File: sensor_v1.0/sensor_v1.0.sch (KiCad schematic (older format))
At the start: 4 parts

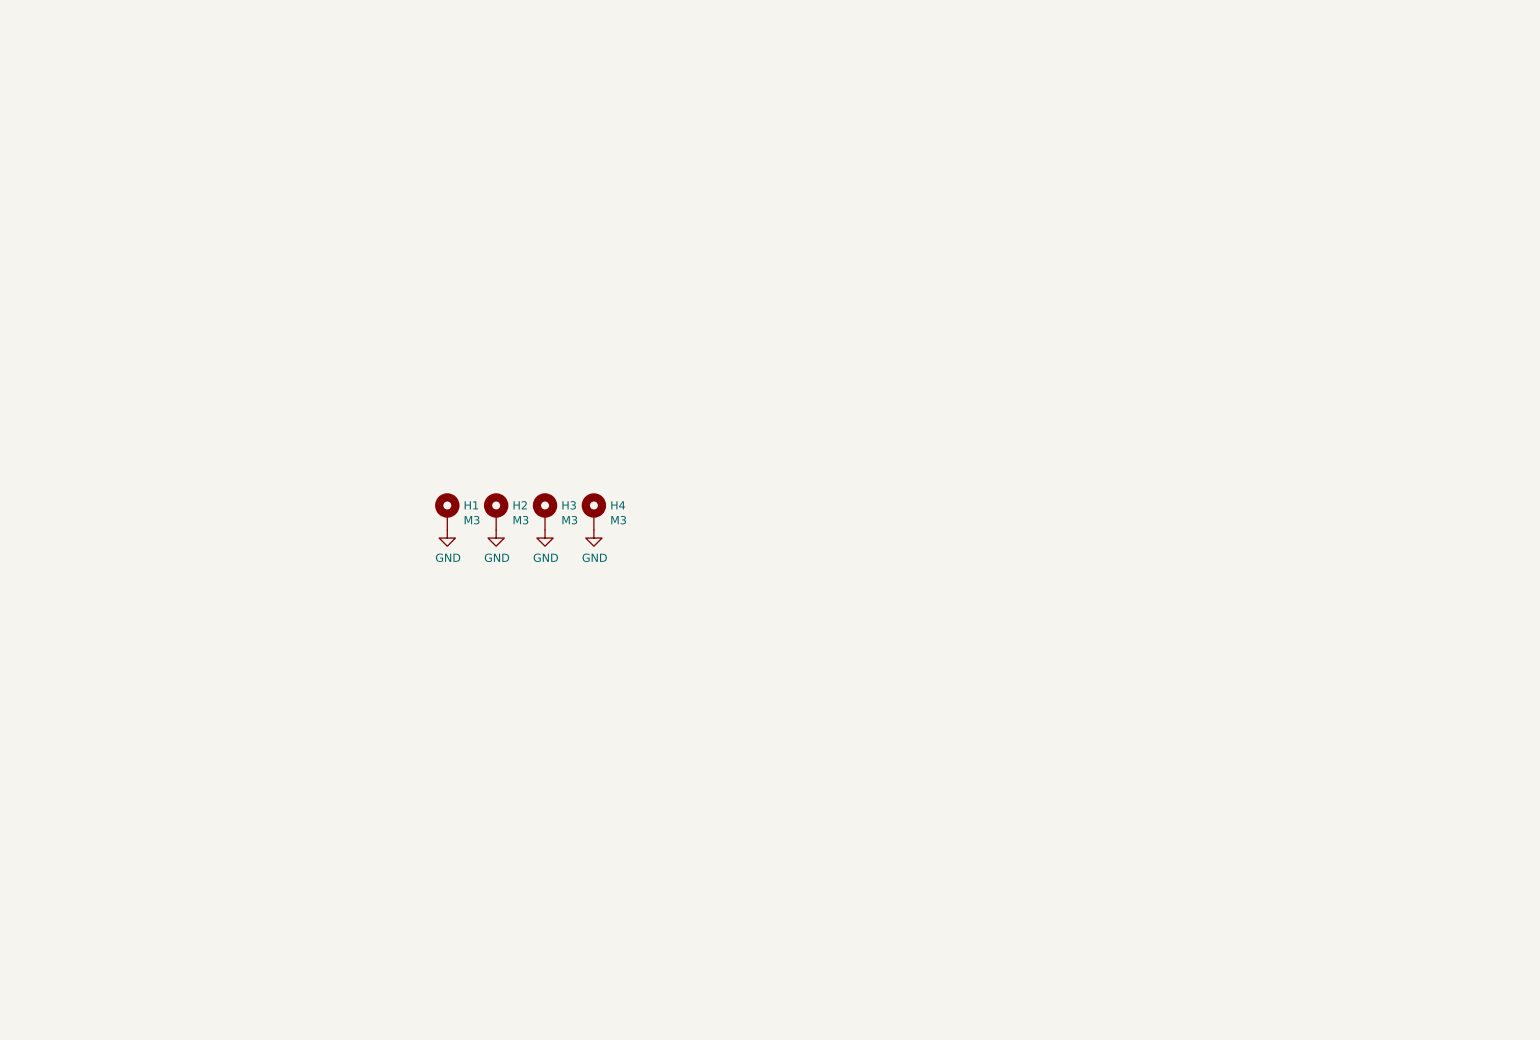
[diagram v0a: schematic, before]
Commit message: sensor board v1.0 mostly routed
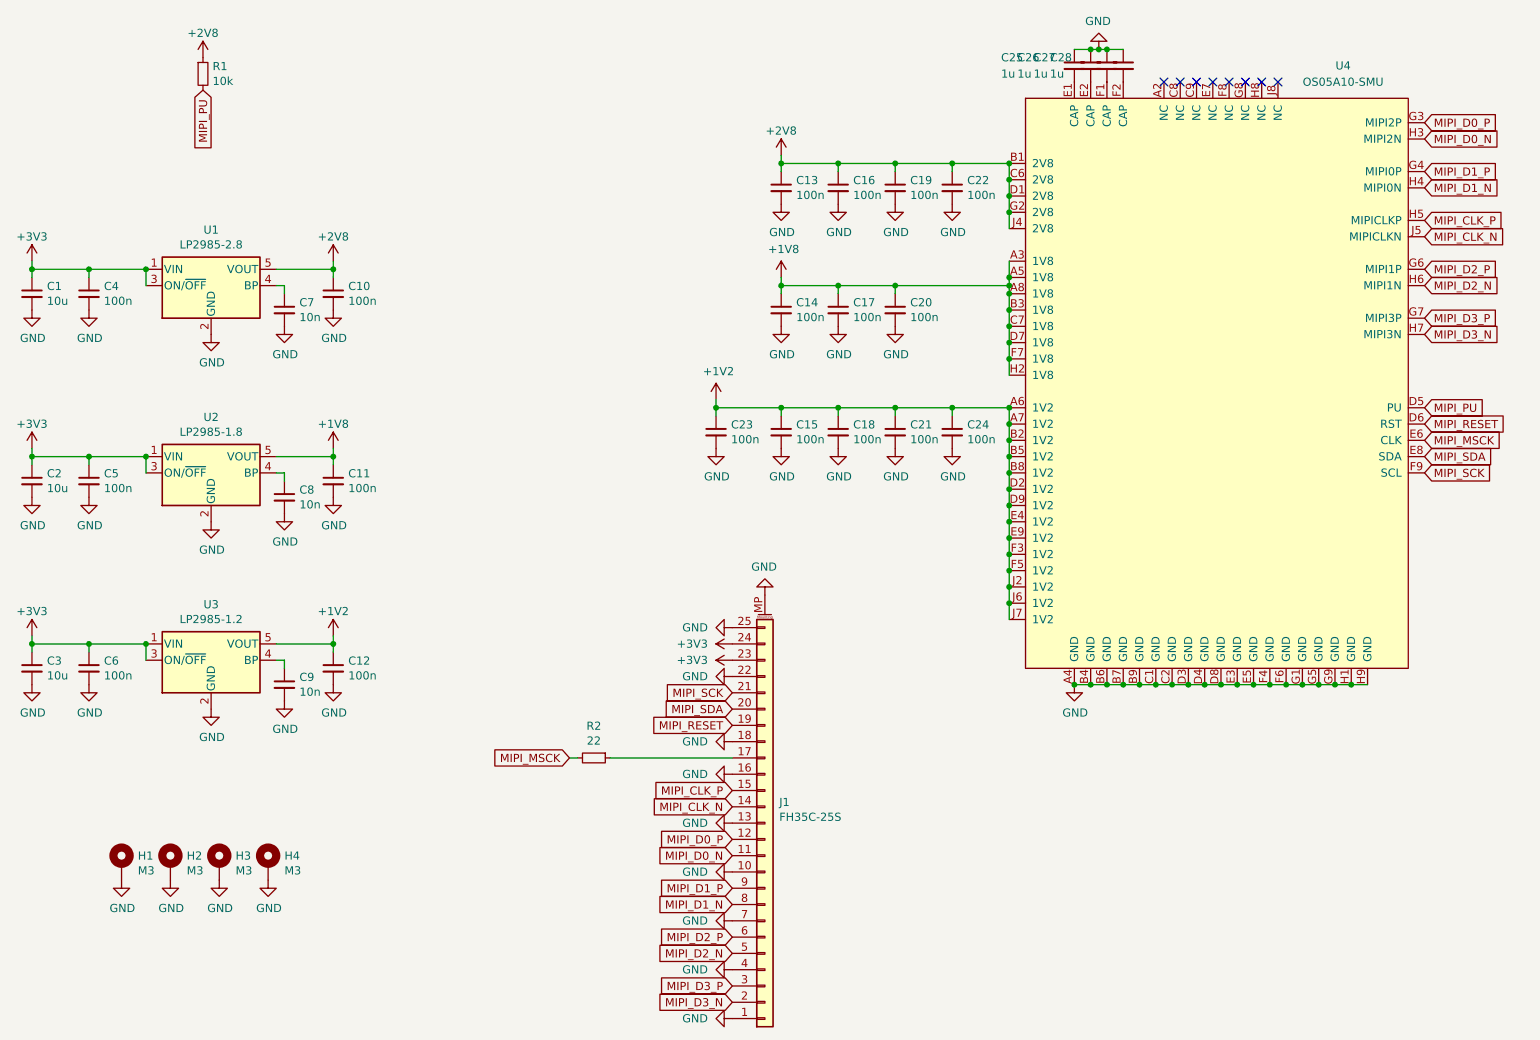
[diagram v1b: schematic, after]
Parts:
- added C1, C2, C3: 10u, otter:C_0603, symbol Device:C_Small
- added C10, C11, C12, C13, C14, C15, C16, C17, C18, C19, C20, C21, C22, C23, C24, C4, C5, C6: 100n, otter:C_0402, symbol Device:C_Small
- added C25, C26, C27, C28: 1u, otter:C_0402, symbol Device:C_Small
- added C7, C8, C9: 10n, otter:C_0402, symbol Device:C_Small
- added J1: FH35C-25S, otter:FH35C-25S, symbol Connector_Generic_MountingPin:Conn_01x25_MountingPin
- added R1: 10k, otter:R_0402, symbol Device:R_Small
- added R2: 22, otter:R_0402, symbol Device:R_Small
- added U1: LP2985-2.8, Package_TO_SOT_SMD:SOT-23-5, symbol Regulator_Linear:LP2985-2.8
- added U2: LP2985-1.8, Package_TO_SOT_SMD:SOT-23-5, symbol Regulator_Linear:LP2985-1.8
- added U3: LP2985-1.2, Package_TO_SOT_SMD:SOT-23-5, symbol Regulator_Linear:LP2985-1.8
- added U4: OS05A10-SMU, otter:OS05A10, symbol otter:OS05A10-SMU
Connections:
- net GND: now also C1.2, C10.2, C11.2, C12.2, C13.2, C14.2, C15.2, C16.2, C17.2, C18.2, C19.2, C2.2, C20.2, C21.2, C22.2, C23.2, C24.2, C25.1, C26.1, C27.1, C28.1, C3.2, C4.2, C5.2, C6.2, C7.2, C8.2, C9.2, J1.1 (Pin_1), J1.10 (Pin_10), J1.13 (Pin_13), J1.16 (Pin_16), J1.18 (Pin_18), J1.22 (Pin_22), J1.25 (Pin_25), J1.4 (Pin_4), J1.7 (Pin_7), J1.MP (MountPin), U1.2 (GND), U2.2 (GND), U3.2 (GND), U4.A4 (GND), U4.B4 (GND), U4.B6 (GND), U4.B7 (GND), U4.B9 (GND), U4.C1 (GND), U4.C2 (GND), U4.D3 (GND), U4.D4 (GND), U4.D8 (GND), U4.E3 (GND), U4.E5 (GND), U4.F4 (GND), U4.F6 (GND), U4.G1 (GND), U4.G5 (GND), U4.G9 (GND), U4.H1 (GND), U4.H9 (GND)
- new net: C25.2, U4.E1 (CAP)
- new net: C26.2, U4.E2 (CAP)
- new net: C27.2, U4.F1 (CAP)
- new net: C28.2, U4.F2 (CAP)
- new net: J1.17 (Pin_17), R2.1
- new net: C7.1, U1.4 (BP)
- new net: C8.1, U2.4 (BP)
- new net: C9.1, U3.4 (BP)
- new net +1V2: C12.1, C15.1, C18.1, C21.1, C23.1, C24.1, U3.5 (VOUT), U4.A6 (1V2), U4.A7 (1V2), U4.B2 (1V2), U4.B5 (1V2), U4.B8 (1V2), U4.D2 (1V2), U4.D9 (1V2), U4.E4 (1V2), U4.E9 (1V2), U4.F3 (1V2), U4.F5 (1V2), U4.J2 (1V2), U4.J6 (1V2), U4.J7 (1V2)
- new net +1V8: C11.1, C14.1, C17.1, C20.1, U2.5 (VOUT), U4.A3 (1V8), U4.A5 (1V8), U4.A8 (1V8), U4.B3 (1V8), U4.C7 (1V8), U4.D7 (1V8), U4.F7 (1V8), U4.H2 (1V8)
- new net +2V8: C10.1, C13.1, C16.1, C19.1, C22.1, R1.1, U1.5 (VOUT), U4.B1 (2V8), U4.C6 (2V8), U4.D1 (2V8), U4.G2 (2V8), U4.J4 (2V8)
- new net +3V3: C1.1, C2.1, C3.1, C4.1, C5.1, C6.1, J1.23 (Pin_23), J1.24 (Pin_24), U1.1 (VIN), U1.3 (ON/~OFF~), U2.1 (VIN), U2.3 (ON/~OFF~), U3.1 (VIN), U3.3 (ON/~OFF~)
- new net MIPI_CLK_N: J1.14 (Pin_14), U4.J5 (MIPICLKN)
- new net MIPI_CLK_P: J1.15 (Pin_15), U4.H5 (MIPICLKP)
- new net MIPI_D0_N: J1.11 (Pin_11), U4.H3 (MIPI2N)
- new net MIPI_D0_P: J1.12 (Pin_12), U4.G3 (MIPI2P)
- new net MIPI_D1_N: J1.8 (Pin_8), U4.H4 (MIPI0N)
- new net MIPI_D1_P: J1.9 (Pin_9), U4.G4 (MIPI0P)
- new net MIPI_D2_N: J1.5 (Pin_5), U4.H6 (MIPI1N)
- new net MIPI_D2_P: J1.6 (Pin_6), U4.G6 (MIPI1P)
- new net MIPI_D3_N: J1.2 (Pin_2), U4.H7 (MIPI3N)
- new net MIPI_D3_P: J1.3 (Pin_3), U4.G7 (MIPI3P)
- new net MIPI_MSCK: R2.2, U4.E6 (CLK)
- new net MIPI_PU: R1.2, U4.D5 (PU)
- new net MIPI_RESET: J1.19 (Pin_19), U4.D6 (RST)
- new net MIPI_SCK: J1.21 (Pin_21), U4.F9 (SCL)
- new net MIPI_SDA: J1.20 (Pin_20), U4.E8 (SDA)
- no-connect marks 0 -> 8
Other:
- moved on the sheet: H1, H2, H3, H4

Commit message: routing 100%
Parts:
- removed C13: 100n, otter:C_0402, symbol Device:C_Small
- added C29: 100n, otter:C_0402, symbol Device:C_Small
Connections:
- net +1V2: now also C29.1
- net GND: now also C29.2
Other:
- moved on the sheet: C16, C19, C22, C23
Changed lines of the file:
@@
 L power:+1V2 #PWR0121
 U 1 1 6099D00B
-P 5000 3500
-F 0 "#PWR0121" H 5000 3350 50  0001 C CNN
-F 1 "+1V2" H 5015 3673 50  0000 C CNN
-F 2 "" H 5000 3500 50  0001 C CNN
-F 3 "" H 5000 3500 50  0001 C CNN
-	1    5000 3500
+P 4700 3500
+F 0 "#PWR0121" H 4700 3350 50  0001 C CNN
+F 1 "+1V2" H 4715 3673 50  0000 C CNN
+F 2 "" H 4700 3500 50  0001 C CNN
+F 3 "" H 4700 3500 50  0001 C CNN
+	1    4700 3500
 	1    0    0    -1
 $EndComp
@@
 L Device:C_Small C22
 U 1 1 609E55E9
-P 6450 2200
-F 0 "C22" H 6542 2246 50  0000 L CNN
-F 1 "100n" H 6542 2155 50  0000 L CNN
-F 2 "otter:C_0402" H 6450 2200 50  0001 C CNN
-F 3 "~" H 6450 2200 50  0001 C CNN
-	1    6450 2200
-	1    0    0    -1
-$EndComp
-$Comp
-L otter:GND #PWR0143
-U 1 1 609E55EF
-P 6450 2300
-F 0 "#PWR0143" H 6450 2050 50  0001 C CNN
-F 1 "GND" H 6455 2127 50  0000 C CNN
-F 2 "" H 6450 2300 60  0000 C CNN
-F 3 "" H 6450 2300 60  0000 C CNN
-	1    6450 2300
-	1    0    0    -1
-$EndComp
-Wire Wire Line
-	6450 2100 6450 2050
-$Comp
-L Device:C_Small C19
-U 1 1 609E7EA2
 P 6100 2200
-F 0 "C19" H 6192 2246 50  0000 L CNN
+F 0 "C22" H 6192 2246 50  0000 L CNN
 F 1 "100n" H 6192 2155 50  0000 L CNN
 F 2 "otter:C_0402" H 6100 2200 50  0001 C CNN
@@
 $EndComp
 $Comp
-L otter:GND #PWR0144
-U 1 1 609E7EA8
+L otter:GND #PWR0143
+U 1 1 609E55EF
 P 6100 2300
-F 0 "#PWR0144" H 6100 2050 50  0001 C CNN
+F 0 "#PWR0143" H 6100 2050 50  0001 C CNN
 F 1 "GND" H 6105 2127 50  0000 C CNN
 F 2 "" H 6100 2300 60  0000 C CNN
@@
 	6100 2100 6100 2050
 $Comp
-L Device:C_Small C16
-U 1 1 609EAC1B
+L Device:C_Small C19
+U 1 1 609E7EA2
 P 5750 2200
-F 0 "C16" H 5842 2246 50  0000 L CNN
+F 0 "C19" H 5842 2246 50  0000 L CNN
 F 1 "100n" H 5842 2155 50  0000 L CNN
 F 2 "otter:C_0402" H 5750 2200 50  0001 C CNN
@@
 $EndComp
 $Comp
-L otter:GND #PWR0145
-U 1 1 609EAC21
+L otter:GND #PWR0144
+U 1 1 609E7EA8
 P 5750 2300
-F 0 "#PWR0145" H 5750 2050 50  0001 C CNN
+F 0 "#PWR0144" H 5750 2050 50  0001 C CNN
 F 1 "GND" H 5755 2127 50  0000 C CNN
 F 2 "" H 5750 2300 60  0000 C CNN
@@
 	5750 2100 5750 2050
 $Comp
-L Device:C_Small C13
-U 1 1 609ED9E9
+L Device:C_Small C16
+U 1 1 609EAC1B
 P 5400 2200
-F 0 "C13" H 5492 2246 50  0000 L CNN
+F 0 "C16" H 5492 2246 50  0000 L CNN
 F 1 "100n" H 5492 2155 50  0000 L CNN
 F 2 "otter:C_0402" H 5400 2200 50  0001 C CNN
@@
 $EndComp
 $Comp
-L otter:GND #PWR0146
-U 1 1 609ED9EF
+L otter:GND #PWR0145
+U 1 1 609EAC21
 P 5400 2300
-F 0 "#PWR0146" H 5400 2050 50  0001 C CNN
+F 0 "#PWR0145" H 5400 2050 50  0001 C CNN
 F 1 "GND" H 5405 2127 50  0000 C CNN
 F 2 "" H 5400 2300 60  0000 C CNN
@@
 Connection ~ 6100 2050
 Wire Wire Line
-	6100 2050 6450 2050
-Wire Wire Line
 	5400 2000 5400 2050
-Connection ~ 6450 2050
-Wire Wire Line
-	6450 2050 6800 2050
-Connection ~ 5400 2050
 Connection ~ 5750 2050
 Wire Wire Line
@@
 L Device:C_Small C23
 U 1 1 60A20C1F
-P 5000 3700
-F 0 "C23" H 5092 3746 50  0000 L CNN
-F 1 "100n" H 5092 3655 50  0000 L CNN
-F 2 "otter:C_0402" H 5000 3700 50  0001 C CNN
-F 3 "~" H 5000 3700 50  0001 C CNN
-	1    5000 3700
+P 5050 3700
+F 0 "C23" H 5142 3746 50  0000 L CNN
+F 1 "100n" H 5142 3655 50  0000 L CNN
+F 2 "otter:C_0402" H 5050 3700 50  0001 C CNN
+F 3 "~" H 5050 3700 50  0001 C CNN
+	1    5050 3700
 	1    0    0    -1
 $EndComp
@@
 L otter:GND #PWR0147
 U 1 1 60A20C25
-P 5000 3800
-F 0 "#PWR0147" H 5000 3550 50  0001 C CNN
-F 1 "GND" H 5005 3627 50  0000 C CNN
-F 2 "" H 5000 3800 60  0000 C CNN
-F 3 "" H 5000 3800 60  0000 C CNN
-	1    5000 3800
+P 5050 3800
+F 0 "#PWR0147" H 5050 3550 50  0001 C CNN
+F 1 "GND" H 5055 3627 50  0000 C CNN
+F 2 "" H 5050 3800 60  0000 C CNN
+F 3 "" H 5050 3800 60  0000 C CNN
+	1    5050 3800
 	1    0    0    -1
 $EndComp
@@
 	6100 2800 6800 2800
 Wire Wire Line
-	5000 3500 5000 3550
-Wire Wire Line
-	5000 3550 5400 3550
-Connection ~ 5000 3550
-Wire Wire Line
-	5000 3550 5000 3600
+	5050 3550 5050 3600
 Connection ~ 5400 3550
+$Comp
+L Device:C_Small C29
+U 1 1 60B46212
+P 4700 3700
+F 0 "C29" H 4792 3746 50  0000 L CNN
+F 1 "100n" H 4792 3655 50  0000 L CNN
+F 2 "otter:C_0402" H 4700 3700 50  0001 C CNN
+F 3 "~" H 4700 3700 50  0001 C CNN
+	1    4700 3700
+	1    0    0    -1
+$EndComp
+$Comp
+L otter:GND #PWR0156
+U 1 1 60B46218
+P 4700 3800
+F 0 "#PWR0156" H 4700 3550 50  0001 C CNN
+F 1 "GND" H 4705 3627 50  0000 C CNN
+F 2 "" H 4700 3800 60  0000 C CNN
+F 3 "" H 4700 3800 60  0000 C CNN
+	1    4700 3800
+	1    0    0    -1
+$EndComp
+Connection ~ 5050 3550
+Wire Wire Line
+	5050 3550 5400 3550
+Wire Wire Line
+	4700 3500 4700 3550
+Wire Wire Line
+	4700 3550 5050 3550
+Connection ~ 4700 3550
+Wire Wire Line
+	4700 3550 4700 3600
+Connection ~ 5400 2050
+Wire Wire Line
+	6100 2050 6800 2050
 $EndSCHEMATC

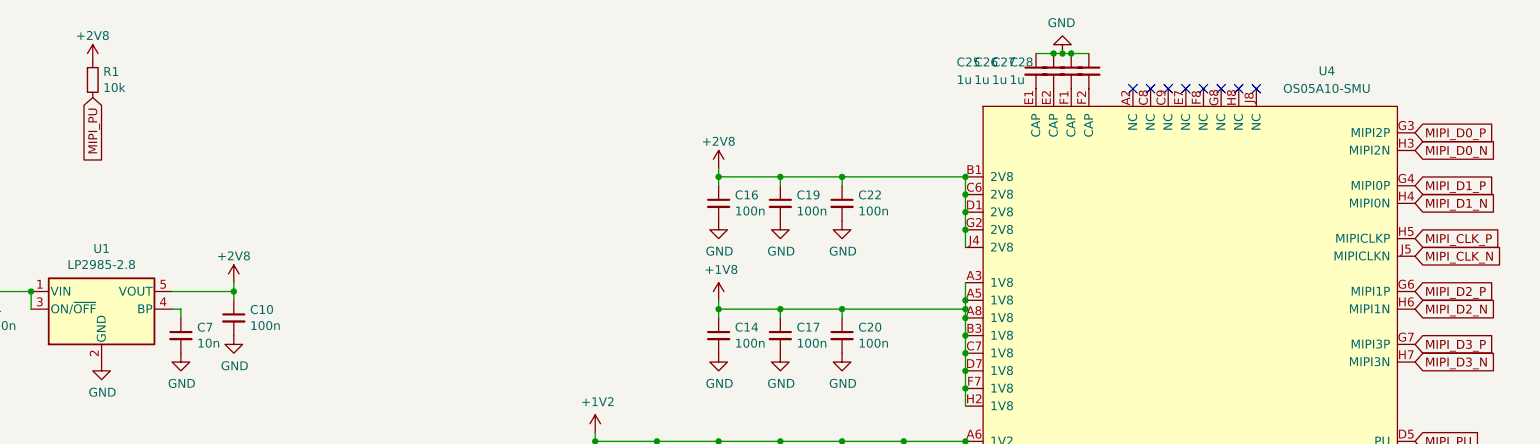
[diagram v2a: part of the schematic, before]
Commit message: fixed MIPI pinout, added pullups, fixed silkscreen
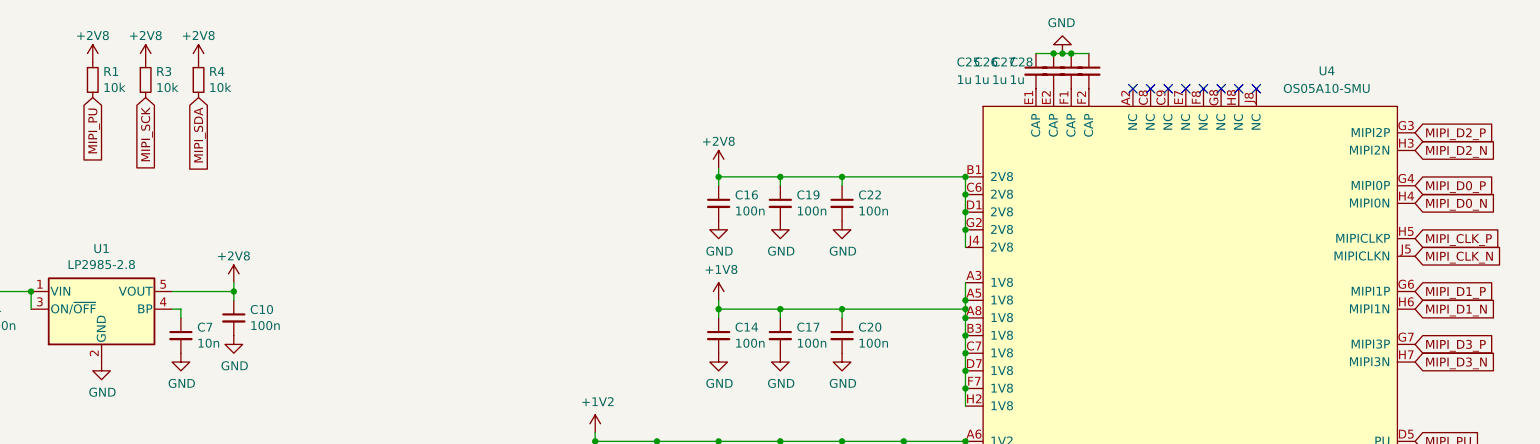
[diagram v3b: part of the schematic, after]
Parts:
- added R3, R4: 10k, otter:R_0402, symbol Device:R_Small
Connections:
- net +2V8: now also R3.1, R4.1
- net MIPI_D0_N: now also U4.H4 (MIPI0N); no longer U4.H3 (MIPI2N)
- net MIPI_D0_P: now also U4.G4 (MIPI0P); no longer U4.G3 (MIPI2P)
- net MIPI_D1_N: now also U4.H6 (MIPI1N); no longer U4.H4 (MIPI0N)
- net MIPI_D1_P: now also U4.G6 (MIPI1P); no longer U4.G4 (MIPI0P)
- net MIPI_D2_N: now also U4.H3 (MIPI2N); no longer U4.H6 (MIPI1N)
- net MIPI_D2_P: now also U4.G3 (MIPI2P); no longer U4.G6 (MIPI1P)
- net MIPI_SCK: now also R3.2
- net MIPI_SDA: now also R4.2
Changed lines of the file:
@@
 	0    -1   -1   0
 $EndComp
-Text GLabel 9350 1800 2    50   Input ~ 0
+Text GLabel 9350 2100 2    50   Input ~ 0
 MIPI_D0_P
-Text GLabel 9350 1900 2    50   Input ~ 0
+Text GLabel 9350 2200 2    50   Input ~ 0
 MIPI_D0_N
 Text GLabel 9350 2400 2    50   Input ~ 0
@@
 Text GLabel 9350 2500 2    50   Input ~ 0
 MIPI_CLK_N
-Text GLabel 9350 2100 2    50   Input ~ 0
+Text GLabel 9350 2700 2    50   Input ~ 0
 MIPI_D1_P
-Text GLabel 9350 2200 2    50   Input ~ 0
+Text GLabel 9350 2800 2    50   Input ~ 0
 MIPI_D1_N
-Text GLabel 9350 2700 2    50   Input ~ 0
+Text GLabel 9350 1800 2    50   Input ~ 0
 MIPI_D2_P
-Text GLabel 9350 2800 2    50   Input ~ 0
+Text GLabel 9350 1900 2    50   Input ~ 0
 MIPI_D2_N
 Text GLabel 9350 3000 2    50   Input ~ 0
@@
 Wire Wire Line
 	6100 2050 6800 2050
+Text GLabel 2150 1600 3    50   Input ~ 0
+MIPI_SCK
+Text GLabel 2450 1600 3    50   Input ~ 0
+MIPI_SDA
+$Comp
+L Device:R_Small R3
+U 1 1 6168DC5F
+P 2150 1500
+F 0 "R3" H 2209 1546 50  0000 L CNN
+F 1 "10k" H 2209 1455 50  0000 L CNN
+F 2 "otter:R_0402" H 2150 1500 50  0001 C CNN
+F 3 "~" H 2150 1500 50  0001 C CNN
+	1    2150 1500
+	1    0    0    -1
+$EndComp
+$Comp
+L power:+2V8 #PWR0146
+U 1 1 6168DC65
+P 2150 1400
+F 0 "#PWR0146" H 2150 1250 50  0001 C CNN
+F 1 "+2V8" H 2150 1550 50  0000 C CNN
+F 2 "" H 2150 1400 50  0001 C CNN
+F 3 "" H 2150 1400 50  0001 C CNN
+	1    2150 1400
+	1    0    0    -1
+$EndComp
+$Comp
+L Device:R_Small R4
+U 1 1 61691912
+P 2450 1500
+F 0 "R4" H 2509 1546 50  0000 L CNN
+F 1 "10k" H 2509 1455 50  0000 L CNN
+F 2 "otter:R_0402" H 2450 1500 50  0001 C CNN
+F 3 "~" H 2450 1500 50  0001 C CNN
+	1    2450 1500
+	1    0    0    -1
+$EndComp
+$Comp
+L power:+2V8 #PWR0157
+U 1 1 61691918
+P 2450 1400
+F 0 "#PWR0157" H 2450 1250 50  0001 C CNN
+F 1 "+2V8" H 2450 1550 50  0000 C CNN
+F 2 "" H 2450 1400 50  0001 C CNN
+F 3 "" H 2450 1400 50  0001 C CNN
+	1    2450 1400
+	1    0    0    -1
+$EndComp
 $EndSCHEMATC
